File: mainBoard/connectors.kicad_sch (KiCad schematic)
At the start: 37 parts, among them J10 Conn_01x06, J11 Conn_01x07, J12 Conn_01x04, J13 Conn_01x04, J15 Conn_02x05_Odd_Even, J16 Conn_01x02, J17 Conn_01x06, J7 Conn_01x02, J8 Conn_01x02, J9 Conn_01x02, K1 Relay_SPDT, Q3 IRLML6244TRPBF, Q4 IRLML6244TRPBF, Q5 IRLML6244TRPBF, Q6 IRLML6244TRPBF, Q7 IRLML6244TRPBF

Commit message: board routing nearly complete
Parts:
- J17: value Conn_01x06 -> Conn_01x05; footprint Connector_PinHeader_2.54mm:PinHeader_1x06_P2.54mm_Vertical -> Connector_PinHeader_2.54mm:PinHeader_1x05_P2.54mm_Vertical; symbol Connector_Generic:Conn_01x06 -> Connector_Generic:Conn_01x05
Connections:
- net PB12: now reaches J17.1 (Pin_1)
- removed net PB0: J17.6 (Pin_6)
- net PB1 renamed PC6
- net PB2 renamed PB15
- net PC8 renamed PB13
- net PC9 renamed PB14
- no-connect marks 3 -> 2
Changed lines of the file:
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@@
 	)
 	(no_connect
-		(at 152.4 207.01)
-	)
-	(no_connect
 		(at 274.32 104.14)
 	)
@@
 		)
 	)
-	(global_label "PB1"
+	(global_label "Fan2"
 		(shape input)
-		(at 152.4 196.85 0)
+		(at 52.07 137.16 180)
 		(fields_autoplaced yes)
 		(effects
@@
 				(size 1.27 1.27)
 			)
-			(justify left)
+			(justify right)
 		)
 		(property "Intersheetrefs" "${INTERSHEET_REFS}"
-			(at 159.1347 196.85 0)
+			(at 44.4887 137.16 0)
 			(hide yes)
 			(show_name no)
@@
 					(size 1.27 1.27)
 				)
-				(justify left)
+				(justify right)
 			)
 		)
 	)
-	(global_label "Fan2"
+	(global_label "KP_Row2"
 		(shape input)
-		(at 52.07 137.16 180)
+		(at 138.43 67.31 0)
 		(fields_autoplaced yes)
 		(effects
@@
 				(size 1.27 1.27)
 			)
-			(justify right)
+			(justify left)
 		)
 		(property "Intersheetrefs" "${INTERSHEET_REFS}"
-			(at 44.4887 137.16 0)
+			(at 149.8818 67.31 0)
 			(hide yes)
 			(show_name no)
@@
 					(size 1.27 1.27)
 				)
-				(justify right)
+				(justify left)
 			)
 		)
 	)
-	(global_label "KP_Row2"
-		(shape input)
-		(at 138.43 67.31 0)
+	(global_label "PB12"
+		(shape bidirectional)
+		(at 152.4 204.47 0)
 		(fields_autoplaced yes)
 		(effects
@@
 		)
 		(property "Intersheetrefs" "${INTERSHEET_REFS}"
-			(at 149.8818 67.31 0)
+			(at 161.4555 204.47 0)
 			(hide yes)
 			(show_name no)
@@
 		)
 	)
-	(global_label "PB0"
-		(shape input)
-		(at 152.4 194.31 0)
+	(global_label "PB13"
+		(shape bidirectional)
+		(at 152.4 201.93 0)
 		(fields_autoplaced yes)
 		(effects
@@
 		)
 		(property "Intersheetrefs" "${INTERSHEET_REFS}"
-			(at 159.1347 194.31 0)
+			(at 161.4555 201.93 0)
 			(hide yes)
 			(show_name no)
@@
 		)
 	)
+	(global_label "PC6"
+		(shape bidirectional)
+		(at 152.4 194.31 0)
+		(fields_autoplaced yes)
+		(effects
+			(font
+				(size 1.27 1.27)
+			)
+			(justify left)
+		)
+		(property "Intersheetrefs" "${INTERSHEET_REFS}"
+			(at 160.246 194.31 0)
+			(hide yes)
+			(show_name no)
+			(do_not_autoplace no)
+			(effects
+				(font
+					(size 1.27 1.27)
+				)
+				(justify left)
+			)
+		)
+	)
 	(global_label "Conv_Fan"
 		(shape input)
@@
 		)
 	)
-	(global_label "KP_Row3"
-		(shape input)
-		(at 138.43 64.77 0)
-		(fields_autoplaced yes)
-		(effects
-			(font
-				(size 1.27 1.27)
-			)
-			(justify left)
-		)
-		(property "Intersheetrefs" "${INTERSHEET_REFS}"
-			(at 149.8818 64.77 0)
-			(hide yes)
-			(show_name no)
-			(do_not_autoplace no)
-			(effects
-				(font
-					(size 1.27 1.27)
-				)
-				(justify left)
-			)
-		)
-	)
-	(global_label "PB2"
-		(shape input)
-		(at 152.4 199.39 0)
+	(global_label "PB15"
+		(shape bidirectional)
+		(at 152.4 196.85 0)
 		(fields_autoplaced yes)
 		(effects
@@
 		)
 		(property "Intersheetrefs" "${INTERSHEET_REFS}"
-			(at 159.1347 199.39 0)
+			(at 161.4555 196.85 0)
 			(hide yes)
 			(show_name no)
@@
 		)
 	)
-	(global_label "PC8"
+	(global_label "KP_Row3"
 		(shape input)
-		(at 152.4 204.47 0)
+		(at 138.43 64.77 0)
 		(fields_autoplaced yes)
 		(effects
@@
 		)
 		(property "Intersheetrefs" "${INTERSHEET_REFS}"
-			(at 159.1347 204.47 0)
+			(at 149.8818 64.77 0)
 			(hide yes)
 			(show_name no)
@@
 		)
 	)
-	(global_label "PC9"
-		(shape input)
-		(at 152.4 201.93 0)
+	(global_label "PB14"
+		(shape bidirectional)
+		(at 152.4 199.39 0)
 		(fields_autoplaced yes)
 		(effects
@@
 		)
 		(property "Intersheetrefs" "${INTERSHEET_REFS}"
-			(at 159.1347 201.93 0)
+			(at 161.4555 199.39 0)
 			(hide yes)
 			(show_name no)
@@
 	)
 	(symbol
-		(lib_id "Connector_Generic:Conn_01x06")
-		(at 147.32 201.93 180)
+		(lib_id "Connector_Generic:Conn_01x05")
+		(at 147.32 199.39 180)
 		(unit 1)
 		(body_style 1)
@@
 		(dnp no)
 		(property "Reference" "J17"
-			(at 144.78 201.9301 0)
+			(at 144.78 199.3901 0)
 			(show_name no)
 			(do_not_autoplace no)
@@
 			)
 		)
-		(property "Value" "Conn_01x06"
-			(at 144.78 199.3901 0)
+		(property "Value" "Conn_01x05"
+			(at 144.78 196.8501 0)
 			(show_name no)
 			(do_not_autoplace no)
@@
 			)
 		)
-		(property "Footprint" "Connector_PinHeader_2.54mm:PinHeader_1x06_P2.54mm_Vertical"
-			(at 147.32 201.93 0)
+		(property "Footprint" "Connector_PinHeader_2.54mm:PinHeader_1x05_P2.54mm_Vertical"
+			(at 147.32 199.39 0)
 			(hide yes)
 			(show_name no)
@@
 		)
 		(property "Datasheet" ""
-			(at 147.32 201.93 0)
+			(at 147.32 199.39 0)
 			(hide yes)
 			(show_name no)
@@
 			)
 		)
-		(property "Description" "Generic connector, single row, 01x06, script generated (kicad-library-utils/schlib/autogen/connector/)"
-			(at 147.32 201.93 0)
+		(property "Description" "Generic connector, single row, 01x05, script generated (kicad-library-utils/schlib/autogen/connector/)"
+			(at 147.32 199.39 0)
 			(hide yes)
 			(show_name no)
@@
 		(pin "2"
 		)
-		(pin "6"
-		)
 		(pin "5"

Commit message: Add ESD protection to headers
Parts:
- added R61, R62: 4.7k, Resistor_SMD:R_0603_1608Metric_Pad0.98x0.95mm_HandSolder, symbol Device:R_US
- added R63, R65: 100, Resistor_SMD:R_0603_1608Metric_Pad0.98x0.95mm_HandSolder, symbol Device:R_US
- added R64: 10k, Resistor_SMD:R_0603_1608Metric_Pad0.98x0.95mm_HandSolder, symbol Device:R_US
- added U16, U17, U21: 100, Resistor_SMD:R_Array_Convex_4x1206, symbol Parallel_Resistor:ParallelArray-4
- added U18: USBLC6-2SC6, Package_TO_SOT_SMD:SOT-23-6, symbol Power_Protection:USBLC6-2SC6
- added U19: USBLC6-4SC6, Package_TO_SOT_SMD:SOT-23-6, symbol Power_Protection:USBLC6-4SC6
- added U20, U5: S14C15-8, Package_SO:SOIC-14_3.9x8.7mm_P1.27mm, symbol SMC_TVS_Arrays:S14C15-8
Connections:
- net +3.3V: now also R61.1, R62.1, U18.5 (VBUS), U19.5 (VBUS)
- net GND: now also R64.2, U18.2 (GND), U19.2 (GND), U20.1, U20.14, U20.7, U20.8, U5.1, U5.14, U5.7, U5.8
- net I2C_CLK: now also R61.2
- net I2C_SDA: now also R62.2
- net KP_Col0: now also U17.6; no longer J11.1 (Pin_1)
- net KP_Col1: now also U17.4; no longer J11.2 (Pin_2)
- net KP_Col2: now also U17.2; no longer J11.3 (Pin_3)
- net KP_Row0: now also U16.8; no longer J11.4 (Pin_4)
- net KP_Row1: now also U16.6; no longer J11.5 (Pin_5)
- net KP_Row2: now also U16.4; no longer J11.6 (Pin_6)
- net KP_Row3: now also U16.2; no longer J11.7 (Pin_7)
- net NRST_SW: now also U18.4 (I/O2), U19.1 (I/O1); no longer J12.2 (Pin_2)
- net PB12: now also U21.8; no longer J17.1 (Pin_1)
- net PB13: now also U21.6; no longer J17.2 (Pin_2)
- net PB14: now also U21.4; no longer J17.3 (Pin_3)
- net PB15: now also U21.2; no longer J17.4 (Pin_4)
- net PC6: now also R65.2; no longer J17.5 (Pin_5)
- net SWDCLK: now also U19.3 (I/O2)
- net SWDIO: now also U19.4 (I/O3)
- net Soft_Power: now also R63.2, R64.1; no longer J12.4 (Pin_4)
- new net ESD_PB12: J17.1 (Pin_1), U20.2, U21.7
- new net ESD_PB13: J17.2 (Pin_2), U20.3, U21.5
- new net ESD_PB14: J17.3 (Pin_3), U20.5, U21.3
- new net ESD_PB15: J17.4 (Pin_4), U20.5, U21.1
- new net ESD_PC6: J17.5 (Pin_5), R65.1, U20.9
- new net KP_ESD_C0: J11.1 (Pin_1), U17.5, U5.2
- new net KP_ESD_C1: J11.2 (Pin_2), U17.3, U5.3
- new net KP_ESD_C2: J11.3 (Pin_3), U17.1, U5.5
- new net KP_ESD_R1: J11.5 (Pin_5), U16.5, U5.9
- new net KP_ESD_R2: J11.6 (Pin_6), U16.3, U5.10
- new net KP_ESD_R3: J11.7 (Pin_7), U16.1, U5.12
- new net KP_ESD_R30: J11.4 (Pin_4), U16.7, U5.5
- new net SOF_PWR_ESD: J12.4 (Pin_4), U18.1 (I/O1)
- new net SOF_PWR_TVS: R63.1, U18.6 (I/O1)
- new net nRST_ESD: J12.2 (Pin_2), U18.3 (I/O2)
- no-connect marks 2 -> 9
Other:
- note added: "I2C OLED"
- note added: "RAVF164DJT100R x2"
- note added: "STLink Programmer"
- moved on the sheet: BZ1, D10, D11, D12, D13, D15, F4, J10, J11, J12, J13, J15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

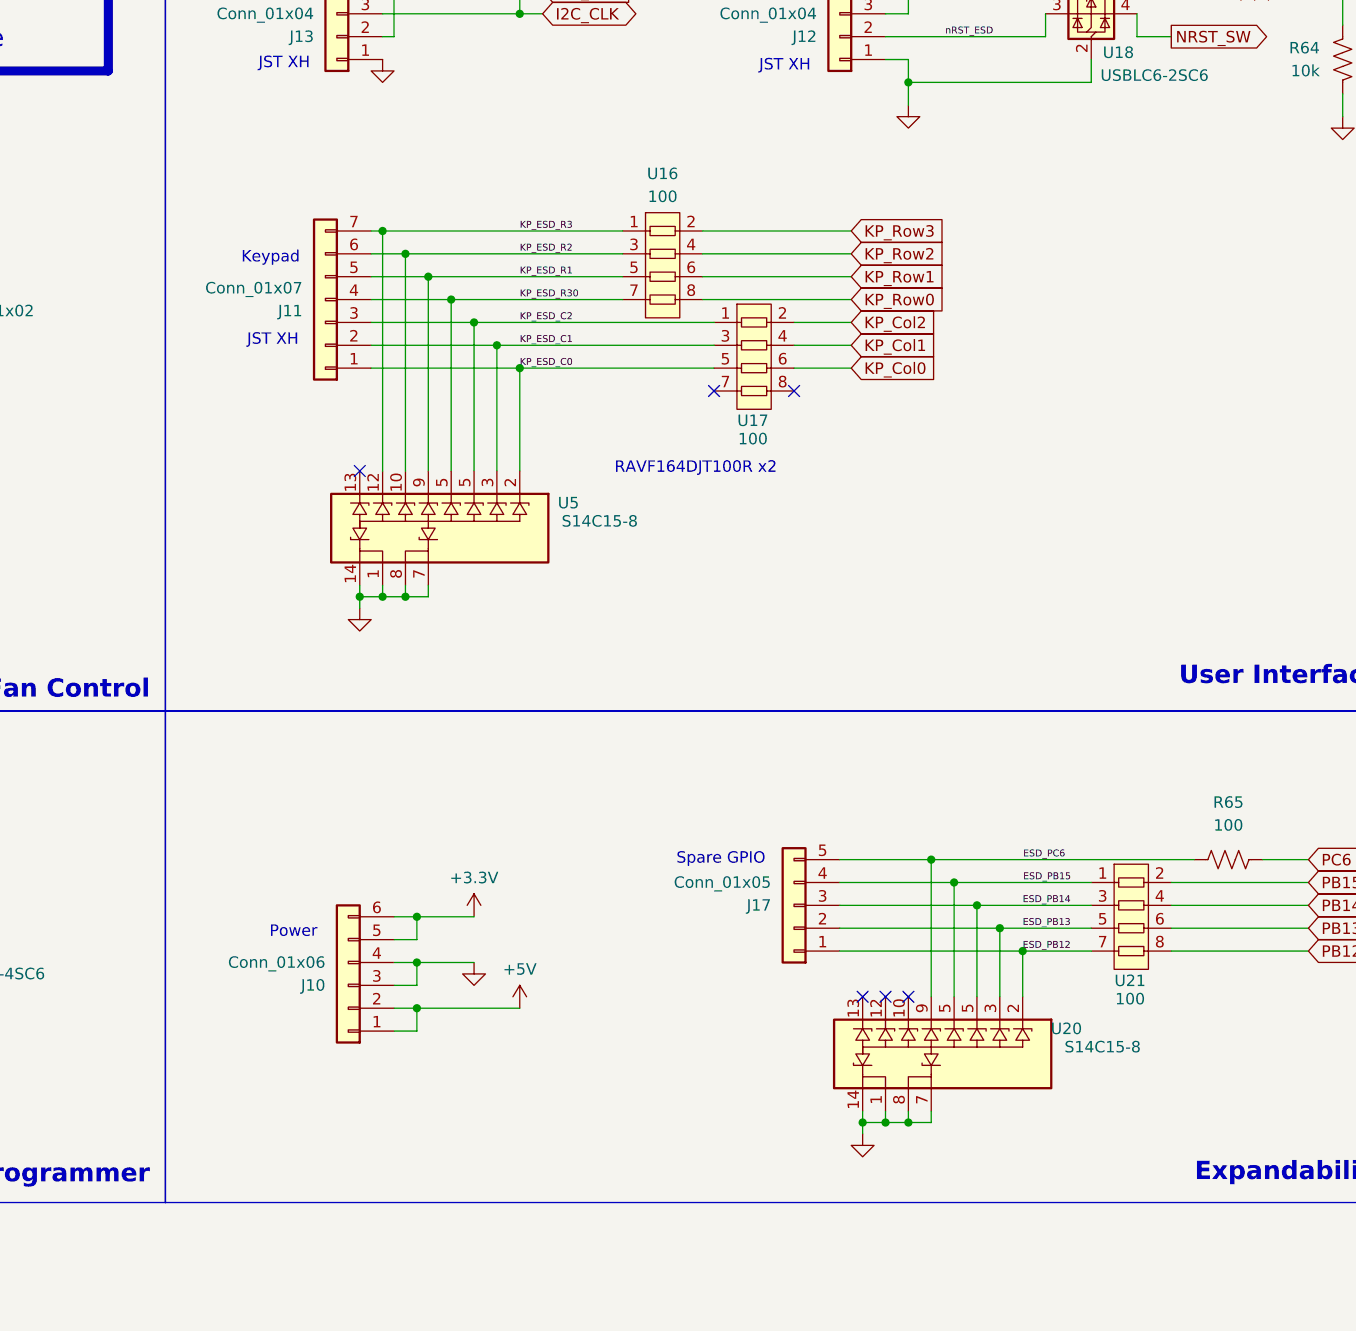
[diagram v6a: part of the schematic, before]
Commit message: change to cheaper ESD TVS diodes
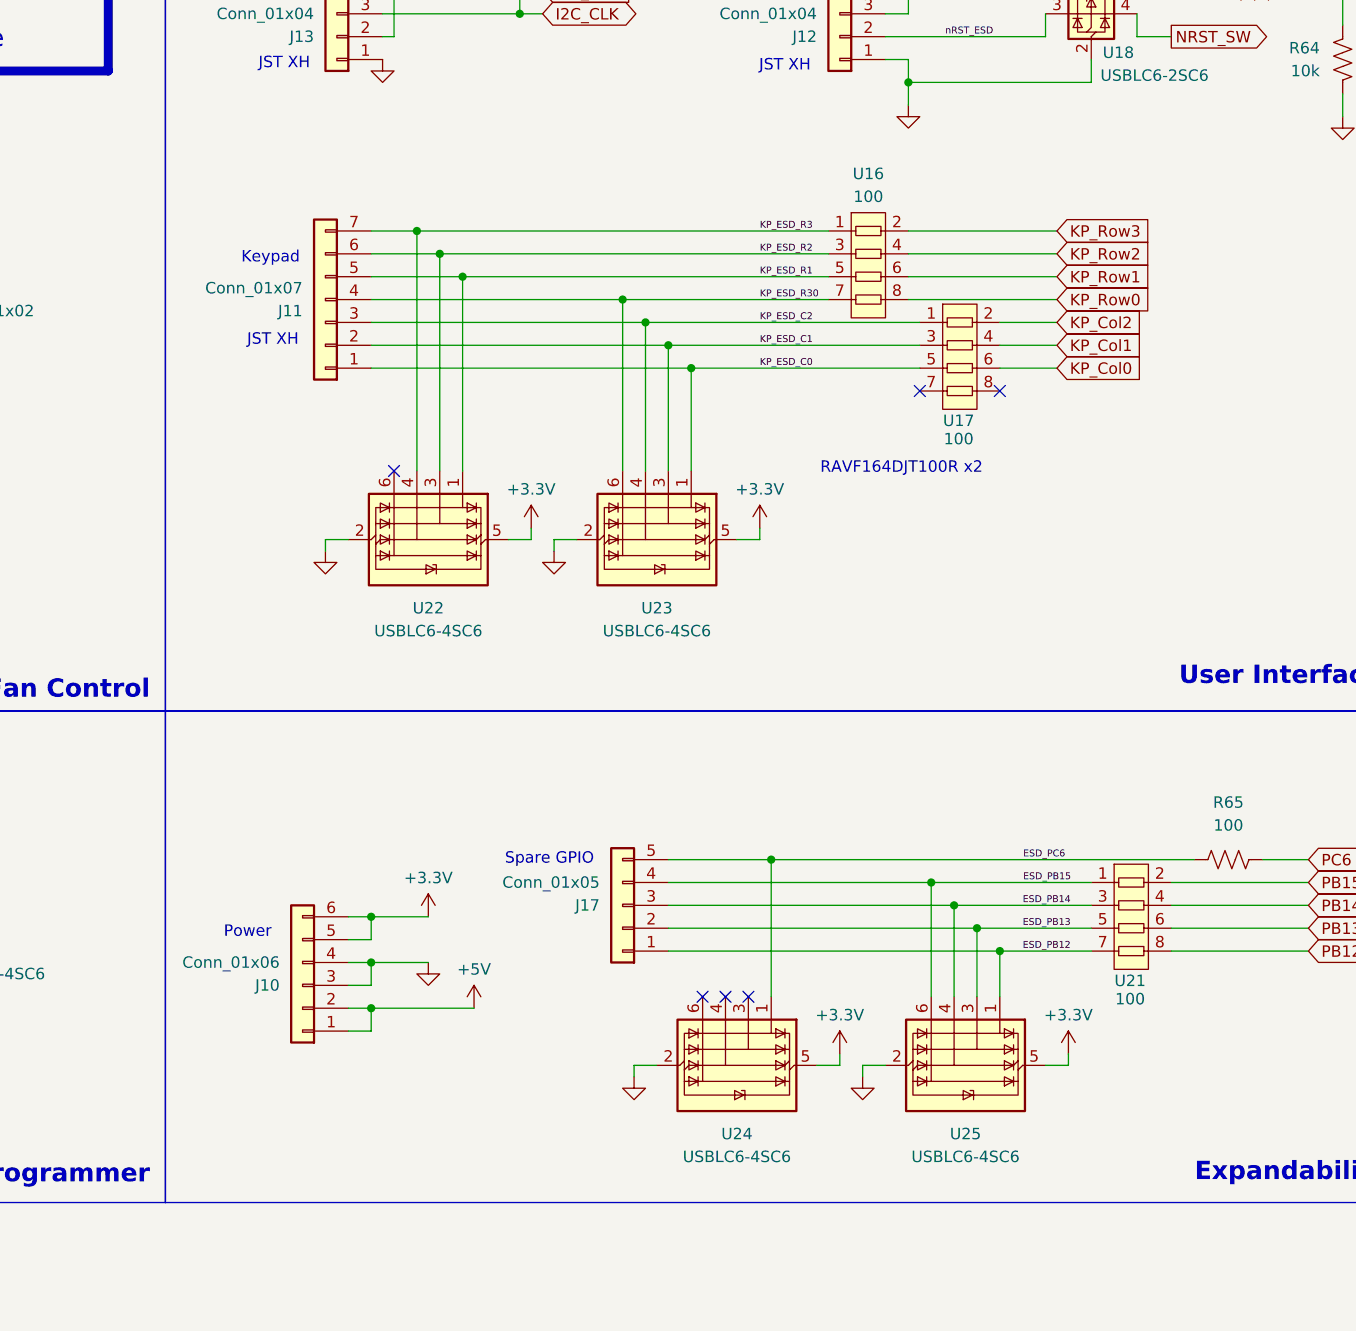
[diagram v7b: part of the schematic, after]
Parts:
- removed U20, U5: S14C15-8, Package_SO:SOIC-14_3.9x8.7mm_P1.27mm, symbol SMC_TVS_Arrays:S14C15-8
- added U22, U23, U24, U25: USBLC6-4SC6, Package_TO_SOT_SMD:SOT-23-6, symbol Power_Protection:USBLC6-4SC6
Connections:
- net +3.3V: now also U22.5 (VBUS), U23.5 (VBUS), U24.5 (VBUS), U25.5 (VBUS)
- net ESD_PB12: now also U25.1 (I/O1)
- net ESD_PB13: now also U25.3 (I/O2)
- net ESD_PB14: now also U25.4 (I/O3)
- net ESD_PB15: now also U25.6 (I/O4)
- net ESD_PC6: now also U24.1 (I/O1)
- net GND: now also U22.2 (GND), U23.2 (GND), U24.2 (GND), U25.2 (GND)
- net KP_ESD_C0: now also U23.1 (I/O1)
- net KP_ESD_C1: now also U23.3 (I/O2)
- net KP_ESD_C2: now also U23.4 (I/O3)
- net KP_ESD_R1: now also U22.1 (I/O1)
- net KP_ESD_R2: now also U22.3 (I/O2)
- net KP_ESD_R3: now also U22.4 (I/O3)
- net KP_ESD_R30: now also U23.6 (I/O4)
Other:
- moved on the sheet: J10, J17, U16, U17

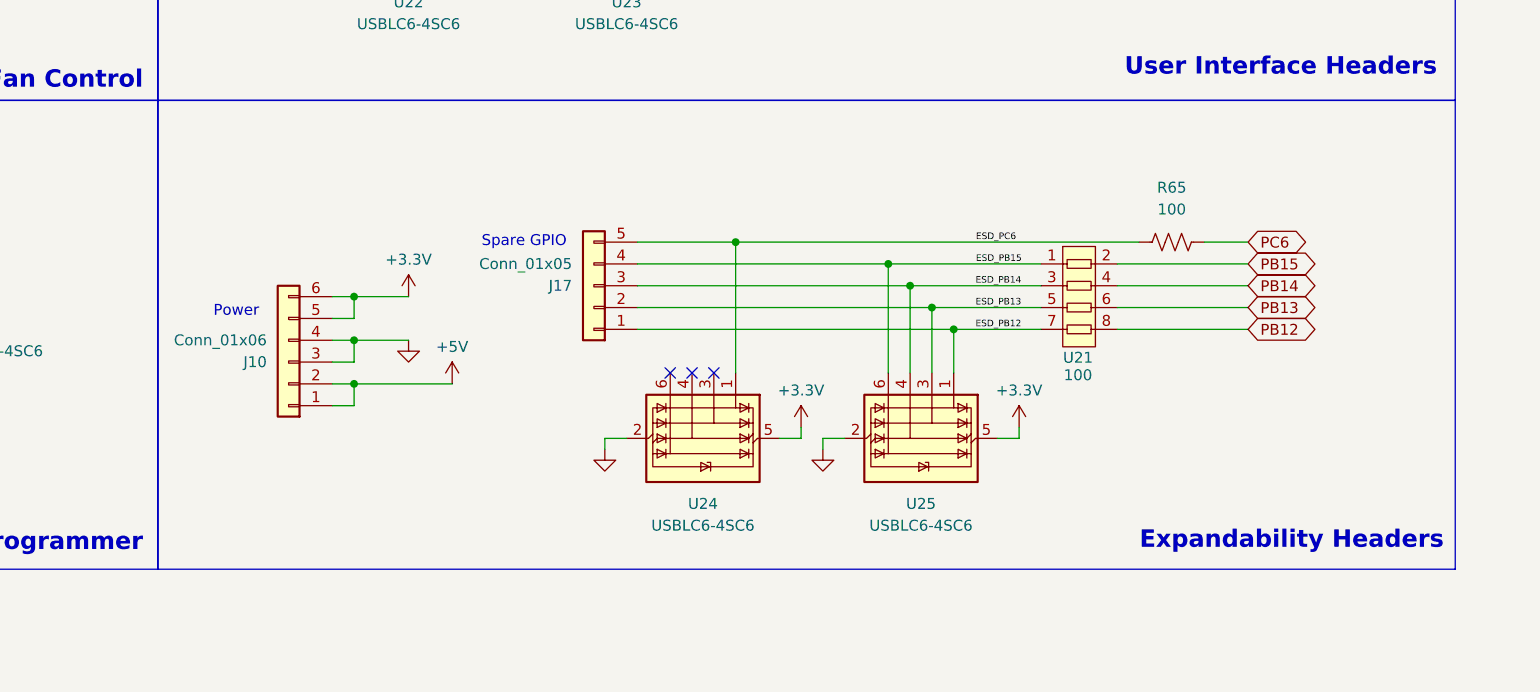
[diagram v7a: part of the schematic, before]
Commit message: Add pullup resistors to digital thermometers
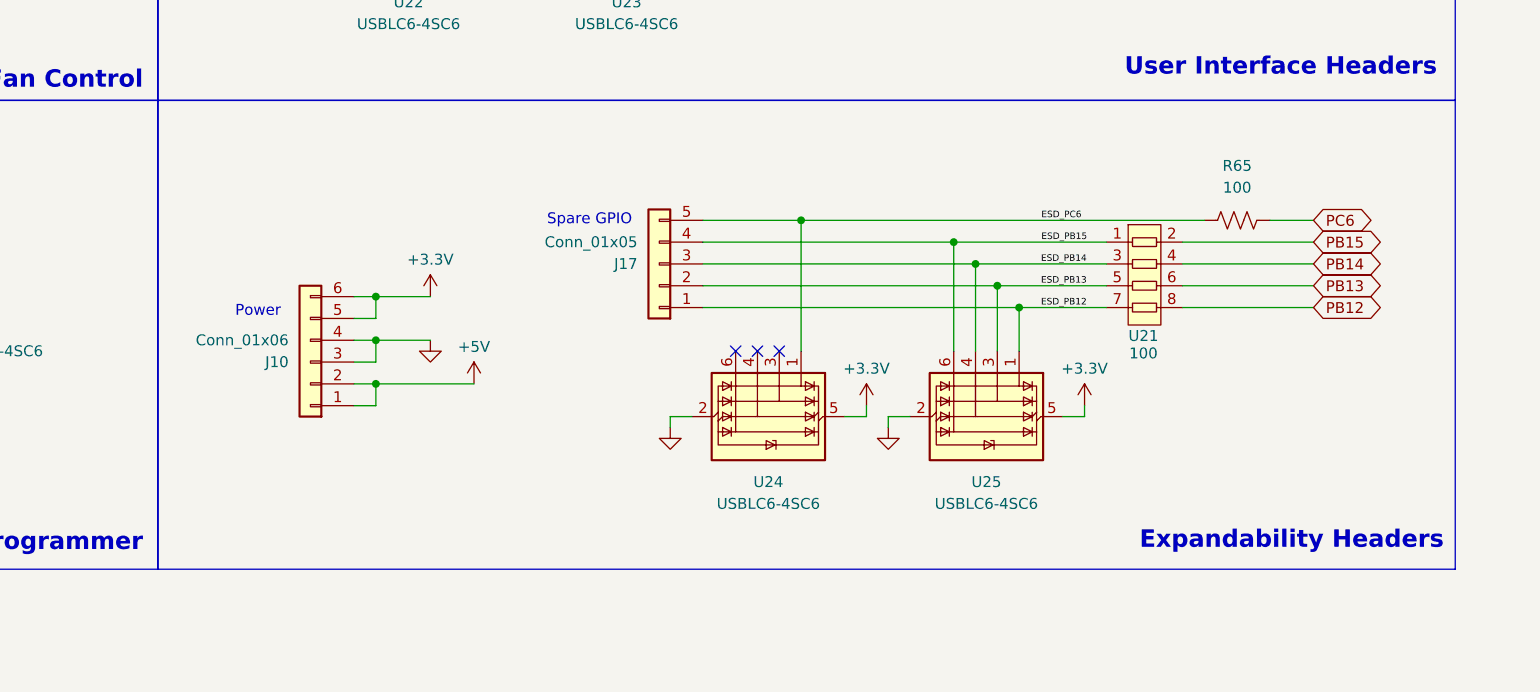
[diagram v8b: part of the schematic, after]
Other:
- moved on the sheet: J10, J17, R65, U21, U24, U25
